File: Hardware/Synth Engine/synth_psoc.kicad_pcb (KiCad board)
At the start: 2 copper layers, 233 parts, among them J1 Barrel_Jack, J10 Conn_01x13, J11 Conn_01x13, J13 Conn_01x05, J14 Conn_01x05, J15 Conn_01x05, J16 Conn_01x05, J2 Audio-Jack-2_Switch, J3 SWD_programming, J4 Conn_01x08, J5 Conn_01x02, J6 Conn_01x03, J7 Capsense_buttons, J8 Conn_01x13, J9 Conn_01x13, Q1 MMBT3904-TP, Q2 MMBT3904-TP, Q3 MMBT3904-TP, Q4 MMBT3904-TP, Q5 MMBFJ177, Q6 MMBFJ177, Q7 MMBFJ177, Q8 MMBFJ177, U1 TL074, U2 TL074, U3 TL074, U4 TL074, U5 TL074, U6 CY8C4246AZI-L445, U7 V7805-1000, U8 PT2399, Y1 Crystal

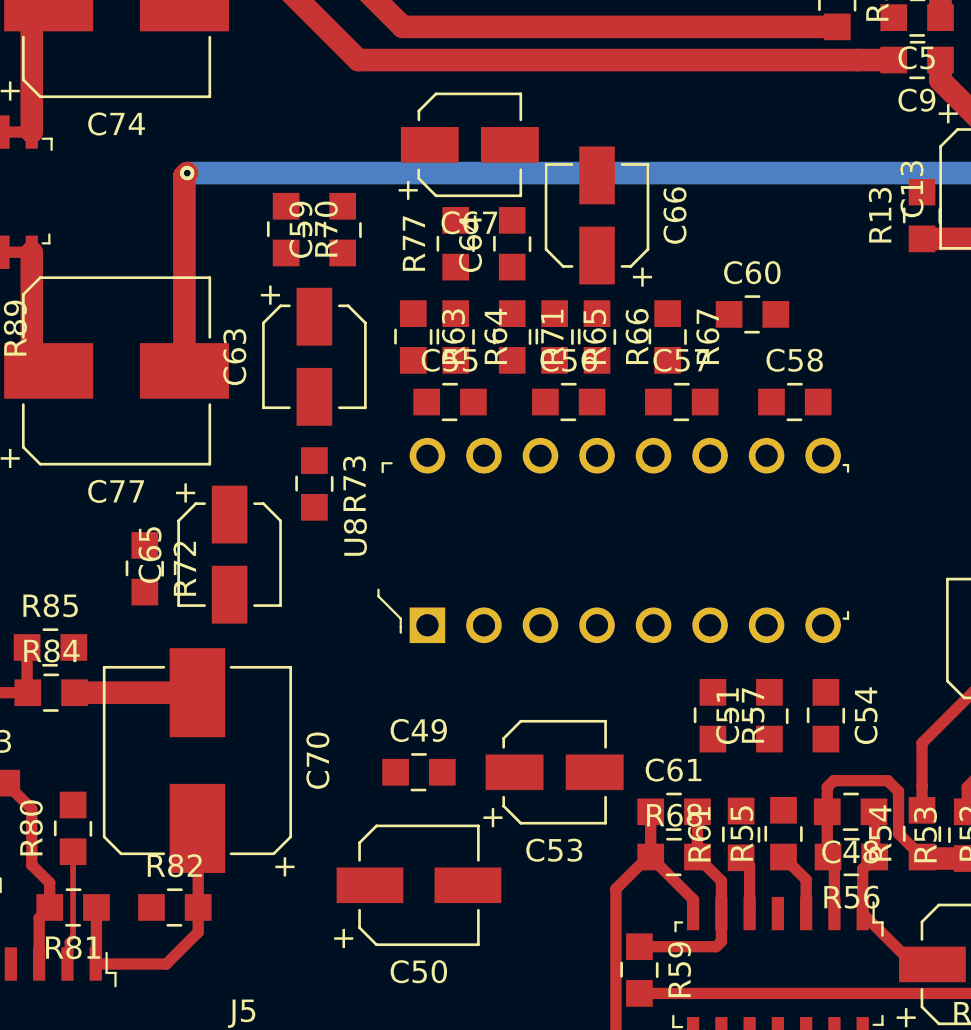
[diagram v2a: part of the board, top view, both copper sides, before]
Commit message: route majority of delay components
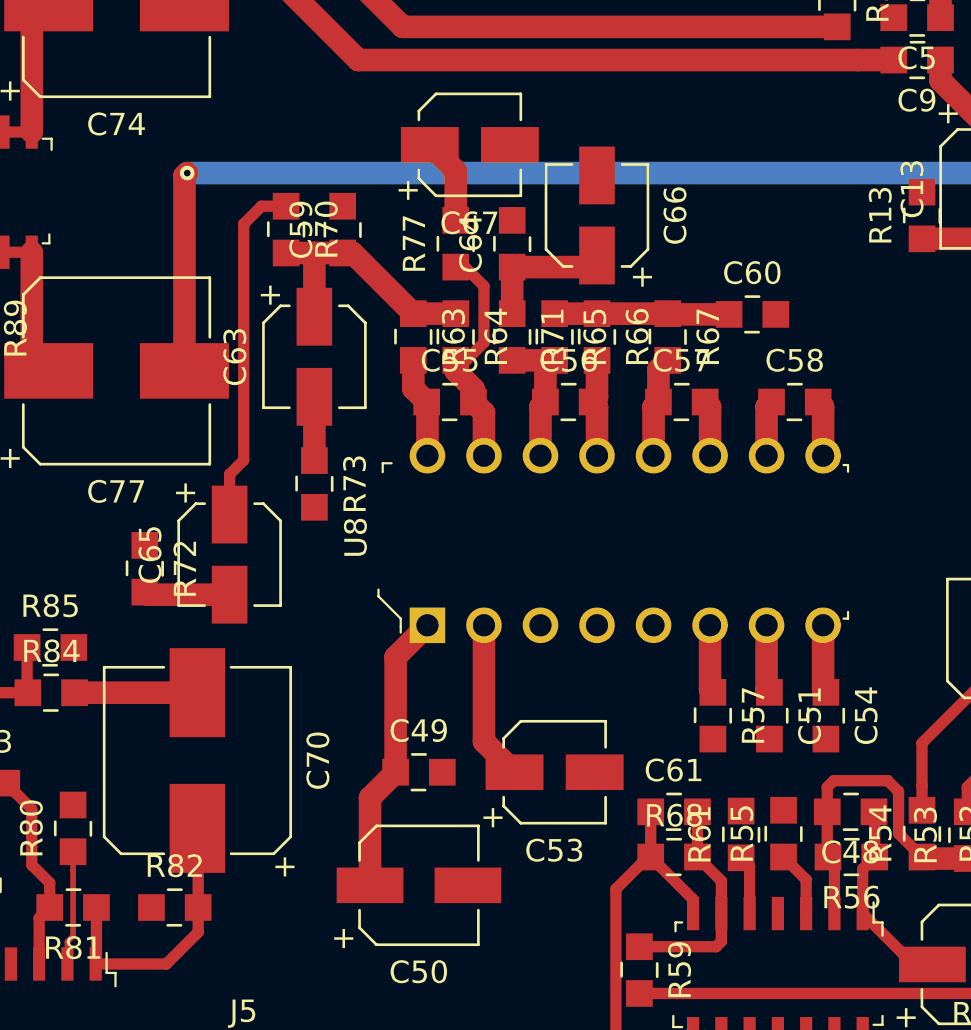
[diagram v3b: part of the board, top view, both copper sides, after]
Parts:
- turned C51 to 270 degrees
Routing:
- net Net-(C65-Pad1): track 0.00 -> 15.6 mm
- net +5V: track 85.7 -> 98.4 mm
- net Net-(C59-Pad1): track 0.00 -> 11.6 mm
- net Net-(C55-Pad2): track 0.00 -> 10.6 mm
- net Net-(C60-Pad1): track 0.00 -> 7.85 mm
- net Net-(C53-Pad1): track 0.00 -> 7.17 mm
- net Net-(C56-Pad1): track 0.00 -> 6.45 mm
- net Net-(C64-Pad1): track 0.00 -> 6.12 mm
- net Net-(C55-Pad1): track 0.00 -> 4.55 mm
- net Net-(C57-Pad1): track 0.00 -> 4.55 mm
- net Net-(C56-Pad2): track 0.00 -> 4.47 mm
- net Net-(C67-Pad1): track 0.00 -> 3.88 mm
- net /Mixer and Effects/delay_in: track 24.7 -> 28.5 mm
- net Net-(R57-Pad1): track 0.00 -> 3.07 mm
- net Net-(C54-Pad1): track 0.00 -> 3.07 mm
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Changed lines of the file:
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@@
     (thickness 1.6)
     (drawings 0)
-    (tracks 998)
+    (tracks 1066)
     (zones 0)
     (modules 233)
@@
   )
   (setup
-    (last_trace_width 0.508)
+    (last_trace_width 1.016)
     (user_trace_width 0.0889)
     (user_trace_width 0.127)
@@
   )
   (module digikey-footprints:0805 (layer F.Cu)
-    (at 52.832 117.094 90)
-    (fp_text reference C51 (at 0 -1.84 90) (layer F.SilkS)
+    (at 52.832 117.094 270)
+    (fp_text reference C51 (at 0 -1.84 270) (layer F.SilkS)
       (effects (font (size 1 1) (thickness 0.15)))
     )
-    (fp_text value 0.1uF (at 0 1.95 90) (layer F.Fab)
+    (fp_text value 0.1uF (at 0 1.95 270) (layer F.Fab)
       (effects (font (size 1 1) (thickness 0.15)))
     )
@@
     (fp_line (start 0.95 -0.675) (end 0.95 0.675) (layer F.Fab) (width 0.12))
     (fp_line (start -0.95 -0.675) (end -0.95 0.675) (layer F.Fab) (width 0.12))
-    (pad 2 smd rect (at 1.05 0 90) (size 1.2 1.2) (layers F.Cu F.Paste F.Mask)
+    (pad 2 smd rect (at 1.05 0 270) (size 1.2 1.2) (layers F.Cu F.Paste F.Mask)
       (net 9 GND))
-    (pad 1 smd rect (at -1.05 0 90) (size 1.2 1.2) (layers F.Cu F.Paste F.Mask)
+    (pad 1 smd rect (at -1.05 0 270) (size 1.2 1.2) (layers F.Cu F.Paste F.Mask)
       (net 71 "Net-(C51-Pad1)"))
   )
@@
   (segment (start 26.4 150.793) (end 26.942 151.335) (width 1.016) (layer F.Cu) (net 23))
   (segment (start 19.948 151.335) (end 26.942 151.335) (width 2.032) (layer F.Cu) (net 23))
+  (segment (start 34.884 124.714) (end 34.884 120.784) (width 1.016) (layer F.Cu) (net 24))
+  (segment (start 34.884 120.784) (end 36.034 119.634) (width 1.016) (layer F.Cu) (net 24))
+  (segment (start 37.465 113.03) (end 36.034 114.461) (width 1.016) (layer F.Cu) (net 24))
+  (segment (start 36.034 114.461) (end 36.034 119.634) (width 1.016) (layer F.Cu) (net 24))
   (segment (start 32.022 151.335) (end 33.106 150.251) (width 1.016) (layer F.Cu) (net 24))
   (segment (start 33.106 150.251) (end 33.106 146.763) (width 1.016) (layer F.Cu) (net 24))
@@
   (segment (start 57.023 125.984) (end 57.023 123.986) (width 0.508) (layer F.Cu) (net 70))
   (segment (start 57.023 123.986) (end 57.565 123.444) (width 0.508) (layer F.Cu) (net 70))
+  (segment (start 52.705 113.03) (end 52.705 115.917) (width 1.016) (layer F.Cu) (net 71))
+  (segment (start 52.705 115.917) (end 52.832 116.044) (width 1.016) (layer F.Cu) (net 71))
+  (segment (start 28.575 111.655) (end 24.88 111.655) (width 1.016) (layer F.Cu) (net 72))
+  (segment (start 24.88 111.655) (end 24.765 111.54) (width 1.016) (layer F.Cu) (net 72))
   (segment (start 66.04 130.81) (end 64.516 132.334) (width 0.508) (layer F.Cu) (net 72))
   (segment (start 64.516 132.334) (end 63.407 132.334) (width 0.508) (layer F.Cu) (net 72))
@@
   (segment (start 46.99 129.574) (end 63.253 129.574) (width 0.508) (layer F.Cu) (net 72))
   (segment (start 63.253 129.574) (end 64.557 128.27) (width 0.508) (layer F.Cu) (net 72))
+  (segment (start 40.005 113.03) (end 40.005 118.259) (width 1.016) (layer F.Cu) (net 73))
+  (segment (start 40.005 118.259) (end 41.38 119.634) (width 1.016) (layer F.Cu) (net 73))
+  (segment (start 55.245 113.03) (end 55.245 115.917) (width 1.016) (layer F.Cu) (net 74))
+  (segment (start 55.245 115.917) (end 55.372 116.044) (width 1.016) (layer F.Cu) (net 74))
+  (segment (start 38.735 101.126) (end 39.209 101.126) (width 0.508) (layer F.Cu) (net 75))
+  (segment (start 39.209 101.126) (end 40.005 100.33) (width 0.508) (layer F.Cu) (net 75))
+  (segment (start 40.005 100.33) (end 40.005 97.79) (width 0.508) (layer F.Cu) (net 75))
+  (segment (start 40.005 97.79) (end 39.15 96.935) (width 0.508) (layer F.Cu) (net 75))
+  (segment (start 39.15 96.935) (end 38.735 96.935) (width 0.508) (layer F.Cu) (net 75))
+  (segment (start 39.531 102.396) (end 38.735 101.6) (width 1.016) (layer F.Cu) (net 75))
+  (segment (start 38.735 101.6) (end 38.735 101.126) (width 1.016) (layer F.Cu) (net 75))
+  (segment (start 39.531 102.997) (end 39.531 102.396) (width 1.016) (layer F.Cu) (net 75))
+  (segment (start 40.005 105.41) (end 40.005 103.471) (width 1.016) (layer F.Cu) (net 75))
+  (segment (start 40.005 103.471) (end 39.531 102.997) (width 1.016) (layer F.Cu) (net 75))
+  (segment (start 37.431 102.997) (end 36.83 102.396) (width 1.016) (layer F.Cu) (net 76))
+  (segment (start 36.83 102.396) (end 36.83 101.126) (width 1.016) (layer F.Cu) (net 76))
+  (segment (start 37.465 105.41) (end 37.465 103.031) (width 1.016) (layer F.Cu) (net 76))
+  (segment (start 37.465 103.031) (end 37.431 102.997) (width 1.016) (layer F.Cu) (net 76))
+  (segment (start 45.085 101.126) (end 45.085 102.777) (width 1.016) (layer F.Cu) (net 77))
+  (segment (start 45.085 102.777) (end 44.865 102.997) (width 1.016) (layer F.Cu) (net 77))
+  (segment (start 45.085 105.41) (end 45.085 103.217) (width 1.016) (layer F.Cu) (net 77))
+  (segment (start 45.085 103.217) (end 44.865 102.997) (width 1.016) (layer F.Cu) (net 77))
+  (segment (start 43.18 101.126) (end 41.275 101.126) (width 1.016) (layer F.Cu) (net 78))
+  (segment (start 42.765 102.997) (end 42.765 101.541) (width 1.016) (layer F.Cu) (net 78))
+  (segment (start 42.765 101.541) (end 43.18 101.126) (width 1.016) (layer F.Cu) (net 78))
+  (segment (start 42.545 105.41) (end 42.545 103.217) (width 1.016) (layer F.Cu) (net 78))
+  (segment (start 42.545 103.217) (end 42.765 102.997) (width 1.016) (layer F.Cu) (net 78))
+  (segment (start 50.165 105.41) (end 50.165 103.217) (width 1.016) (layer F.Cu) (net 79))
+  (segment (start 50.165 103.217) (end 49.945 102.997) (width 1.016) (layer F.Cu) (net 79))
+  (segment (start 47.845 102.997) (end 47.845 101.541) (width 1.016) (layer F.Cu) (net 80))
+  (segment (start 47.845 101.541) (end 48.26 101.126) (width 1.016) (layer F.Cu) (net 80))
+  (segment (start 47.625 105.41) (end 47.625 103.217) (width 1.016) (layer F.Cu) (net 80))
+  (segment (start 47.625 103.217) (end 47.845 102.997) (width 1.016) (layer F.Cu) (net 80))
+  (segment (start 55.245 105.41) (end 55.245 103.217) (width 1.016) (layer F.Cu) (net 81))
+  (segment (start 55.245 103.217) (end 55.025 102.997) (width 1.016) (layer F.Cu) (net 81))
+  (segment (start 52.705 105.41) (end 52.705 103.217) (width 1.016) (layer F.Cu) (net 82))
+  (segment (start 52.705 103.217) (end 52.925 102.997) (width 1.016) (layer F.Cu) (net 82))
+  (segment (start 33.655 96.3) (end 32.385 96.3) (width 1.016) (layer F.Cu) (net 83))
+  (segment (start 32.385 96.3) (end 31.115 96.3) (width 1.016) (layer F.Cu) (net 83))
+  (segment (start 32.385 99.165) (end 32.385 96.3) (width 1.016) (layer F.Cu) (net 83))
+  (segment (start 36.83 99.026) (end 38.735 99.026) (width 1.016) (layer F.Cu) (net 83))
+  (segment (start 33.655 96.3) (end 34.104 96.3) (width 1.016) (layer F.Cu) (net 83))
+  (segment (start 34.104 96.3) (end 36.83 99.026) (width 1.016) (layer F.Cu) (net 83))
+  (segment (start 45.085 99.026) (end 43.18 99.026) (width 1.016) (layer F.Cu) (net 84))
+  (segment (start 48.26 99.026) (end 45.085 99.026) (width 1.016) (layer F.Cu) (net 84))
+  (segment (start 51.02 99.06) (end 48.294 99.06) (width 1.016) (layer F.Cu) (net 84))
+  (segment (start 48.294 99.06) (end 48.26 99.026) (width 1.016) (layer F.Cu) (net 84))
   (segment (start 46.99 127.474) (end 50.441 127.474) (width 0.508) (layer F.Cu) (net 85))
   (segment (start 50.441 127.474) (end 50.673 127.242) (width 0.508) (layer F.Cu) (net 85))
@@
   (segment (start 49.403 131.384) (end 49.403 132.173) (width 0.508) (layer F.Cu) (net 88))
   (segment (start 49.403 132.173) (end 47.972 133.604) (width 0.508) (layer F.Cu) (net 88))
+  (segment (start 32.385 102.765) (end 32.385 105.63) (width 1.016) (layer F.Cu) (net 89))
+  (segment (start 41.275 96.935) (end 41.275 99.026) (width 1.016) (layer F.Cu) (net 90))
+  (segment (start 41.275 96.935) (end 44.565 96.935) (width 1.016) (layer F.Cu) (net 90))
+  (segment (start 44.565 96.935) (end 45.085 96.415) (width 1.016) (layer F.Cu) (net 90))
+  (segment (start 29.21 94.997) (end 29.21 105.612) (width 0.508) (layer F.Cu) (net 91))
+  (segment (start 29.21 105.612) (end 28.575 106.247) (width 0.508) (layer F.Cu) (net 91))
+  (segment (start 28.575 106.247) (end 28.575 108.055) (width 0.508) (layer F.Cu) (net 91))
+  (segment (start 31.115 94.2) (end 30.007 94.2) (width 0.508) (layer F.Cu) (net 91))
+  (segment (start 30.007 94.2) (end 29.21 94.997) (width 0.508) (layer F.Cu) (net 91))
+  (segment (start 38.735 94.835) (end 38.735 92.605) (width 1.016) (layer F.Cu) (net 93))
+  (segment (start 38.735 92.605) (end 37.57 91.44) (width 1.016) (layer F.Cu) (net 93))
   (segment (start 56.134 137.6) (end 58.166 137.6) (width 0.508) (layer F.Cu) (net 95))
   (segment (start 55.592 135.636) (end 55.592 137.058) (width 0.508) (layer F.Cu) (net 95))
@@
   (segment (start 53.467 123.444) (end 54.483 124.46) (width 0.508) (layer F.Cu) (net 133))
   (segment (start 54.483 124.46) (end 54.483 125.984) (width 0.508) (layer F.Cu) (net 133))
+  (segment (start 50.165 113.03) (end 50.165 115.917) (width 1.016) (layer F.Cu) (net 135))
+  (segment (start 50.165 115.917) (end 50.292 116.044) (width 1.016) (layer F.Cu) (net 135))
   (segment (start 51.943 125.984) (end 51.943 123.859) (width 0.508) (layer F.Cu) (net 137))
   (segment (start 51.943 123.859) (end 51.562 123.478) (width 0.508) (layer F.Cu) (net 137))

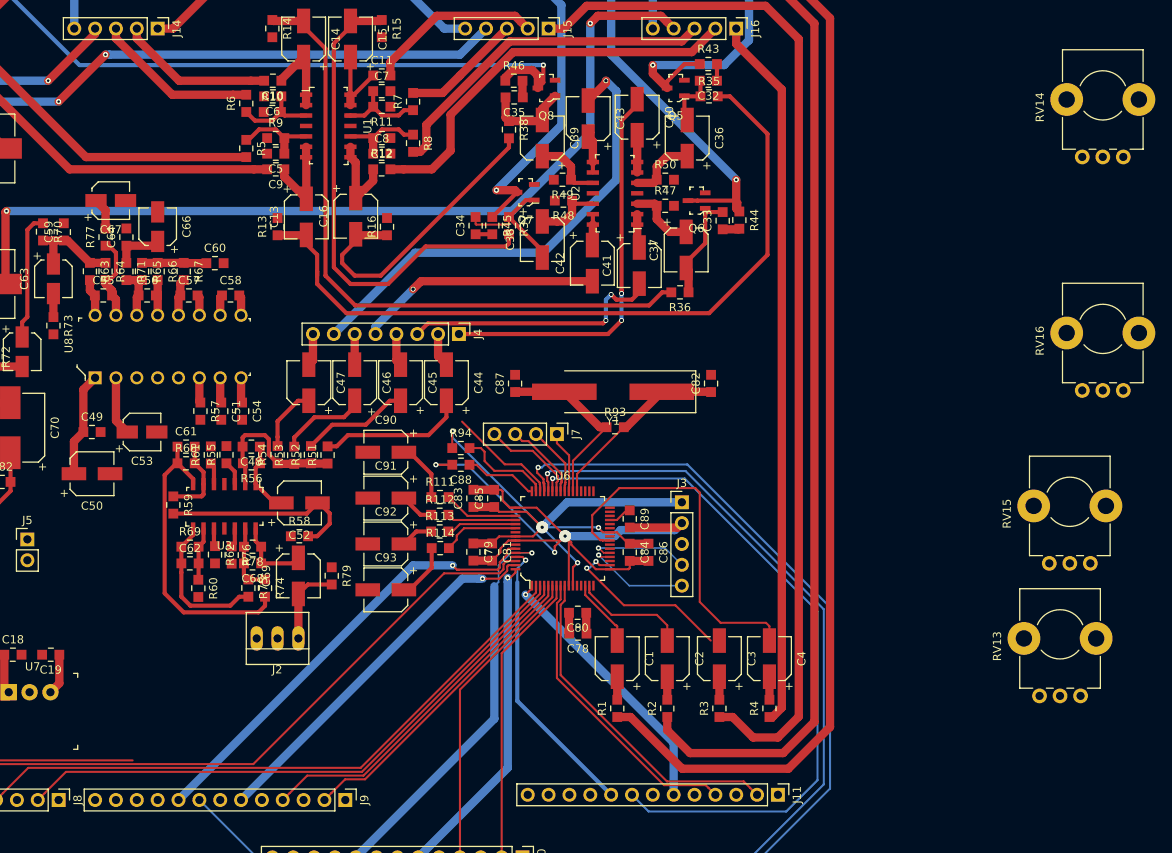
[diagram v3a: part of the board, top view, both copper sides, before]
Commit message: add delay connector to main board and route it.
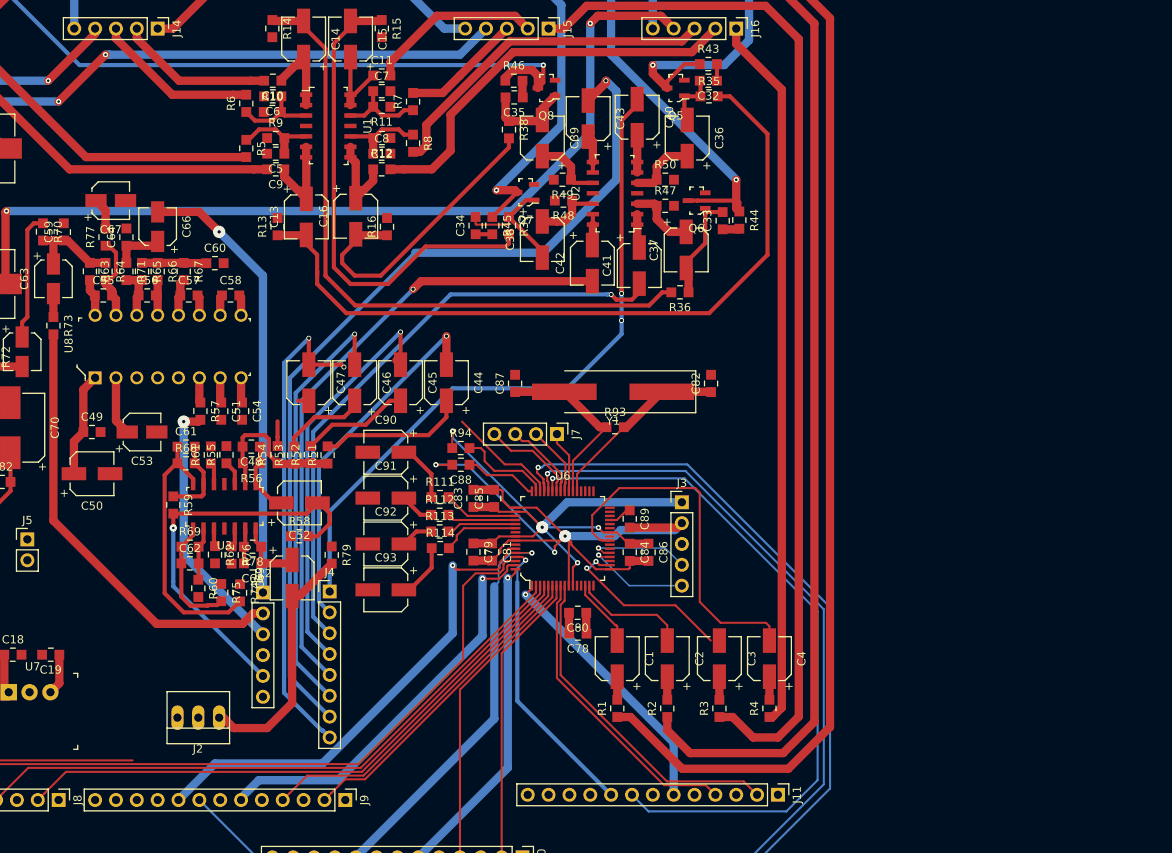
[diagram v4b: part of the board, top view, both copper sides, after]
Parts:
- removed RV13: 20kA, Potentiometers:Potentiometer_Bourns_PTV09A-1_Horizontal
- removed RV14: 20k, Potentiometers:Potentiometer_Bourns_PTV09A-1_Horizontal
- removed RV15, RV16: 50kA, Potentiometers:Potentiometer_Bourns_PTV09A-1_Horizontal
- added J12: Conn_01x06, Pin_Headers:Pin_Header_Straight_1x06_Pitch2.54mm, F.Cu at (57.9, 139.2)
- moved J4 35.1 mm to (66.0, 139.1), turned to 0 degrees
- moved J2 13.6 mm to (52.6, 154.4)
- moved R75 3.35 mm to (52.8, 139.2)
- moved R74 3.10 mm to (55.1, 139.2)
- moved R79 2.54 mm to (66.3, 134.6)
- moved C69 0.80 mm to (61.5, 137.4)
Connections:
- C66 pad 2: Net-(C66-Pad2) -> /Mixer and Effects/delay_fb_ctrl_in
- C67 pad 2: Net-(C67-Pad2) -> /Mixer and Effects/delay_out
- R57 pad 2: Net-(R57-Pad2) -> /Mixer and Effects/delay_time_in
- R73 pad 2: Net-(R73-Pad2) -> /Mixer and Effects/delay_fb_ctrl_out
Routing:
- net /Envelope/env_out_4: track 3.94 -> 59.9 mm, vias 0 -> 2
- net /Mixer and Effects/delay_fb_ctrl_in: track 0.00 -> 54.7 mm, vias 0 -> 1
- net /Mixer and Effects/delay_fb_ctrl_out: track 0.00 -> 54.0 mm
- net Net-(C43-Pad2): track 58.1 -> 108.9 mm
- net /Envelope/env_out_3: track 3.73 -> 52.5 mm, vias 0 -> 1
- net Net-(C42-Pad2): track 29.6 -> 76.3 mm
- net /Envelope/env_out_2: track 3.94 -> 49.8 mm, vias 0 -> 1
- net Net-(C41-Pad2): track 32.6 -> 74.1 mm, vias 2 -> 1
- net /Envelope/env_out_1: track 4.15 -> 44.1 mm, vias 0 -> 1
- net Net-(C40-Pad2): track 48.2 -> 83.7 mm
- net /Mixer and Effects/delay_time_in: track 0.00 -> 32.0 mm, vias 0 -> 1
- net /Mixer and Effects/delay_in: track 28.5 -> 52.8 mm, vias 0 -> 1
- net Net-(C69-Pad2): track 9.96 -> 30.2 mm
- net /Connectors/osc1_speed: track 80.8 -> 86.0 mm
- net /Connectors/osc2_quant: track 54.9 -> 59.7 mm
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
